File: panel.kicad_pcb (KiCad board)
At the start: 2 copper layers, 131.4 x 94 mm, 112 parts, among them J1 Conn_01x05, J2 Conn_01x05, J3 Screw_Terminal

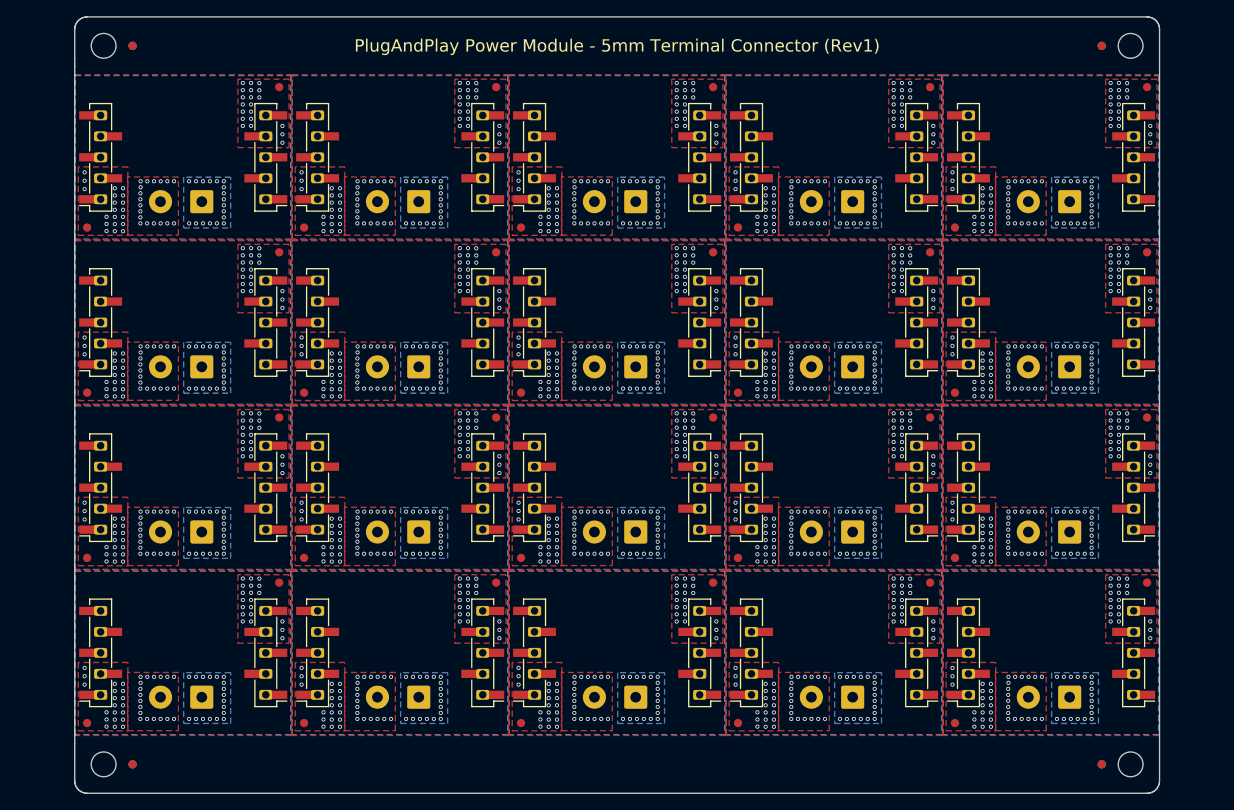
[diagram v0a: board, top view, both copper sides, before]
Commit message: Panel framing on all 4 sides
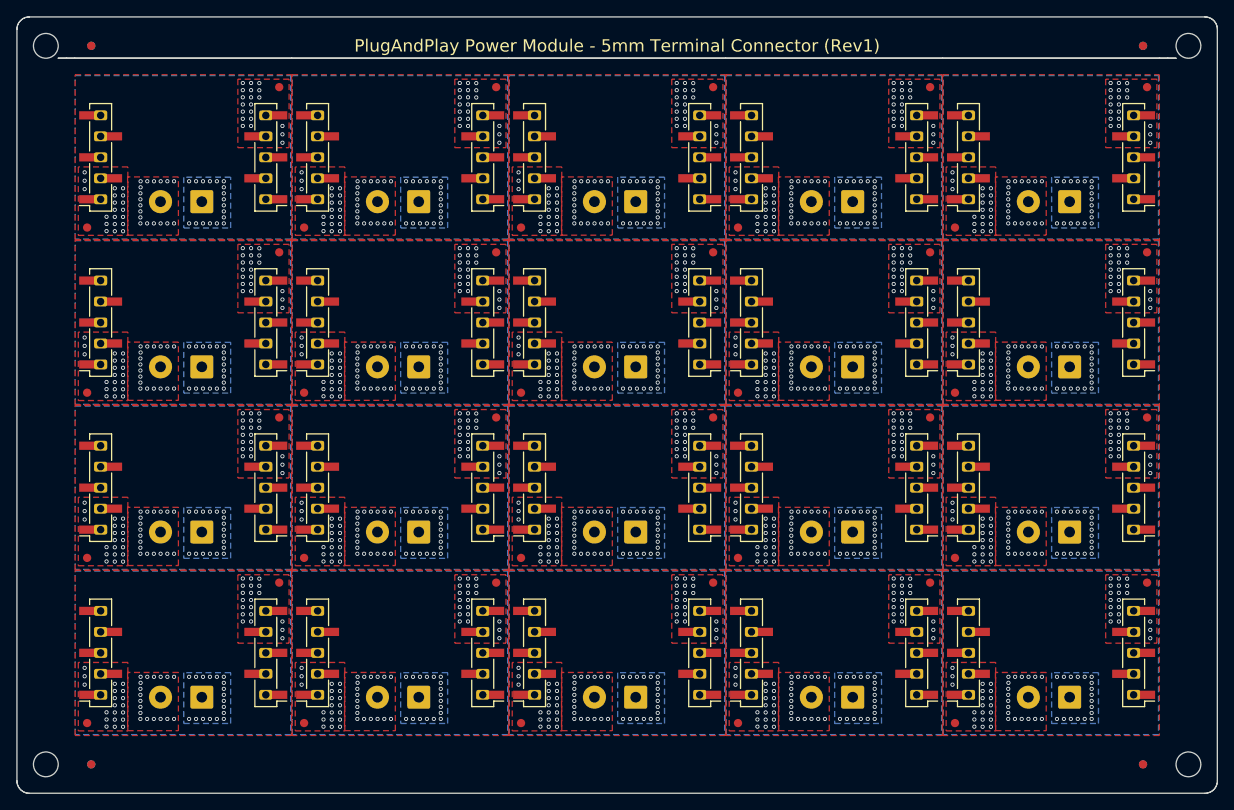
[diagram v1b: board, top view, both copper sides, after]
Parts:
- removed the J1 at (86.0, 57.0)
- removed the J1 at (164.8, 77.0)
- removed the J1 at (86.0, 37.0)
- removed the J1 at (164.8, 37.0)
- removed the J1 at (138.5, 37.0)
- removed the J1 at (112.2, 37.0)
- removed the J1 at (112.2, 57.0)
- removed the J1 at (86.0, 77.0)
- removed the J1 at (112.2, 97.0)
- removed the J1 at (191.0, 77.0)
- removed the J1 at (138.5, 77.0)
- removed the J1 at (138.5, 57.0)
- removed the J1 at (191.0, 37.0)
- removed the J1 at (112.2, 77.0)
- removed the J1 at (86.0, 97.0)
- removed the J1 at (164.8, 57.0)
- removed the J1 at (164.8, 97.0)
- removed the J1 at (191.0, 97.0)
- removed the J1 at (138.5, 97.0)
- removed the J1 at (191.0, 57.0)
- removed the J2 at (132.2, 37.0)
- removed the J2 at (106.0, 57.0)
- removed the J2 at (184.8, 97.0)
- removed the J2 at (158.5, 57.0)
- removed the J2 at (132.2, 77.0)
- removed the J2 at (211.0, 97.0)
- removed the J2 at (132.2, 97.0)
- removed the J2 at (184.8, 77.0)
- removed the J2 at (158.5, 97.0)
- removed the J2 at (132.2, 57.0)
- removed the J2 at (211.0, 57.0)
- removed the J2 at (184.8, 57.0)
- removed the J2 at (106.0, 97.0)
- removed the J2 at (106.0, 77.0)
- removed the J2 at (106.0, 37.0)
- removed the J2 at (184.8, 37.0)
- removed the J2 at (211.0, 37.0)
- removed the J2 at (158.5, 77.0)
- removed the J2 at (158.5, 37.0)
- removed the J2 at (211.0, 77.0)
- removed the J3 at (150.8, 42.4)
- removed the J3 at (124.5, 102.4)
- removed the J3 at (98.2, 82.4)
- removed the J3 at (124.5, 42.4)
- removed the J3 at (177.0, 42.4)
- removed the J3 at (203.3, 82.4)
- removed the J3 at (150.8, 62.4)
- removed the J3 at (124.5, 82.4)
- removed the J3 at (203.3, 102.4)
- removed the J3 at (177.0, 102.4)
- removed the J3 at (177.0, 82.4)
- removed the J3 at (150.8, 82.4)
- removed the J3 at (98.2, 62.4)
- removed the J3 at (98.2, 102.4)
- removed the J3 at (150.8, 102.4)
- removed the J3 at (124.5, 62.4)
- removed the J3 at (98.2, 42.4)
- removed the J3 at (203.3, 62.4)
- removed the J3 at (203.3, 42.4)
- removed the J3 at (177.0, 62.4)
- removed the REF** at (186.4, 68.5)
- removed the REF** at (160.1, 88.5)
- removed the REF** at (186.4, 48.5)
- removed the REF** at (163.1, 65.5)
- removed the REF** at (107.6, 68.5)
- removed the REF** at (212.7, 88.5)
- removed the REF** at (110.6, 65.5)
- removed the REF** at (189.4, 105.5)
- removed the REF** at (84.3, 85.5)
- removed the REF** at (133.9, 88.5)
- removed the REF** at (107.6, 48.5)
- removed the REF** at (84.3, 45.5)
- removed the REF** at (136.9, 85.5)
- removed the REF** at (160.1, 28.5)
- removed the REF** at (163.1, 105.5)
- removed the REF** at (212.7, 68.5)
- removed the REF** at (189.4, 65.5)
- removed the REF** at (110.6, 85.5)
- removed the REF** at (84.3, 105.5)
- removed the REF** at (133.9, 28.5)
- removed the REF** at (212.7, 48.5)
- removed the REF** at (163.1, 45.5)
- removed the REF** at (133.9, 68.5)
- removed the REF** at (110.6, 45.5)
- removed the REF** at (107.6, 88.5)
- removed the REF** at (212.7, 28.5)
- removed the REF** at (136.9, 45.5)
- removed the REF** at (189.4, 45.5)
- removed the REF** at (133.9, 48.5)
- removed the REF** at (160.1, 48.5)
- removed the REF** at (186.4, 88.5)
- removed the REF** at (136.9, 65.5)
- removed the REF** at (136.9, 105.5)
- removed the REF** at (163.1, 85.5)
- removed the REF** at (84.3, 65.5)
- removed the REF** at (160.1, 68.5)
- removed the REF** at (186.4, 28.5)
- removed the REF** at (107.6, 28.5)
- removed the REF** at (110.6, 105.5)
- removed the REF** at (189.4, 85.5)
- added J1: Conn_01x05, Library:PinSocket_1x05_P2.54mm_Vertical_SMD_Pin1Right, F.Cu at (164.8, 37.0)
- added J1: Conn_01x05, Library:PinSocket_1x05_P2.54mm_Vertical_SMD_Pin1Right, F.Cu at (86.0, 57.0)
- added J1: Conn_01x05, Library:PinSocket_1x05_P2.54mm_Vertical_SMD_Pin1Right, F.Cu at (191.0, 37.0)
- added J1: Conn_01x05, Library:PinSocket_1x05_P2.54mm_Vertical_SMD_Pin1Right, F.Cu at (86.0, 97.0)
- added J1: Conn_01x05, Library:PinSocket_1x05_P2.54mm_Vertical_SMD_Pin1Right, F.Cu at (138.5, 77.0)
- added J1: Conn_01x05, Library:PinSocket_1x05_P2.54mm_Vertical_SMD_Pin1Right, F.Cu at (164.8, 57.0)
- added J1: Conn_01x05, Library:PinSocket_1x05_P2.54mm_Vertical_SMD_Pin1Right, F.Cu at (112.2, 97.0)
- added J1: Conn_01x05, Library:PinSocket_1x05_P2.54mm_Vertical_SMD_Pin1Right, F.Cu at (86.0, 77.0)
- added J1: Conn_01x05, Library:PinSocket_1x05_P2.54mm_Vertical_SMD_Pin1Right, F.Cu at (138.5, 97.0)
- added J1: Conn_01x05, Library:PinSocket_1x05_P2.54mm_Vertical_SMD_Pin1Right, F.Cu at (164.8, 77.0)
- added J1: Conn_01x05, Library:PinSocket_1x05_P2.54mm_Vertical_SMD_Pin1Right, F.Cu at (138.5, 57.0)
- added J1: Conn_01x05, Library:PinSocket_1x05_P2.54mm_Vertical_SMD_Pin1Right, F.Cu at (191.0, 77.0)
- added J1: Conn_01x05, Library:PinSocket_1x05_P2.54mm_Vertical_SMD_Pin1Right, F.Cu at (112.2, 77.0)
- added J1: Conn_01x05, Library:PinSocket_1x05_P2.54mm_Vertical_SMD_Pin1Right, F.Cu at (112.2, 57.0)
- added J1: Conn_01x05, Library:PinSocket_1x05_P2.54mm_Vertical_SMD_Pin1Right, F.Cu at (191.0, 57.0)
- added J1: Conn_01x05, Library:PinSocket_1x05_P2.54mm_Vertical_SMD_Pin1Right, F.Cu at (86.0, 37.0)
- added J1: Conn_01x05, Library:PinSocket_1x05_P2.54mm_Vertical_SMD_Pin1Right, F.Cu at (138.5, 37.0)
- added J1: Conn_01x05, Library:PinSocket_1x05_P2.54mm_Vertical_SMD_Pin1Right, F.Cu at (164.8, 97.0)
- added J1: Conn_01x05, Library:PinSocket_1x05_P2.54mm_Vertical_SMD_Pin1Right, F.Cu at (191.0, 97.0)
- added J1: Conn_01x05, Library:PinSocket_1x05_P2.54mm_Vertical_SMD_Pin1Right, F.Cu at (112.2, 37.0)
- added J2: Conn_01x05, Library:PinSocket_1x05_P2.54mm_Vertical_SMD_Pin1Left, F.Cu at (211.0, 77.0)
- added J2: Conn_01x05, Library:PinSocket_1x05_P2.54mm_Vertical_SMD_Pin1Left, F.Cu at (132.2, 97.0)
- added J2: Conn_01x05, Library:PinSocket_1x05_P2.54mm_Vertical_SMD_Pin1Left, F.Cu at (184.8, 97.0)
- added J2: Conn_01x05, Library:PinSocket_1x05_P2.54mm_Vertical_SMD_Pin1Left, F.Cu at (158.5, 37.0)
- added J2: Conn_01x05, Library:PinSocket_1x05_P2.54mm_Vertical_SMD_Pin1Left, F.Cu at (132.2, 37.0)
- added J2: Conn_01x05, Library:PinSocket_1x05_P2.54mm_Vertical_SMD_Pin1Left, F.Cu at (158.5, 77.0)
- added J2: Conn_01x05, Library:PinSocket_1x05_P2.54mm_Vertical_SMD_Pin1Left, F.Cu at (184.8, 57.0)
- added J2: Conn_01x05, Library:PinSocket_1x05_P2.54mm_Vertical_SMD_Pin1Left, F.Cu at (211.0, 37.0)
- added J2: Conn_01x05, Library:PinSocket_1x05_P2.54mm_Vertical_SMD_Pin1Left, F.Cu at (211.0, 57.0)
- added J2: Conn_01x05, Library:PinSocket_1x05_P2.54mm_Vertical_SMD_Pin1Left, F.Cu at (106.0, 97.0)
- added J2: Conn_01x05, Library:PinSocket_1x05_P2.54mm_Vertical_SMD_Pin1Left, F.Cu at (132.2, 77.0)
- added J2: Conn_01x05, Library:PinSocket_1x05_P2.54mm_Vertical_SMD_Pin1Left, F.Cu at (106.0, 37.0)
- added J2: Conn_01x05, Library:PinSocket_1x05_P2.54mm_Vertical_SMD_Pin1Left, F.Cu at (106.0, 77.0)
- added J2: Conn_01x05, Library:PinSocket_1x05_P2.54mm_Vertical_SMD_Pin1Left, F.Cu at (106.0, 57.0)
- added J2: Conn_01x05, Library:PinSocket_1x05_P2.54mm_Vertical_SMD_Pin1Left, F.Cu at (184.8, 77.0)
- added J2: Conn_01x05, Library:PinSocket_1x05_P2.54mm_Vertical_SMD_Pin1Left, F.Cu at (158.5, 97.0)
- added J2: Conn_01x05, Library:PinSocket_1x05_P2.54mm_Vertical_SMD_Pin1Left, F.Cu at (184.8, 37.0)
- added J2: Conn_01x05, Library:PinSocket_1x05_P2.54mm_Vertical_SMD_Pin1Left, F.Cu at (158.5, 57.0)
- added J2: Conn_01x05, Library:PinSocket_1x05_P2.54mm_Vertical_SMD_Pin1Left, F.Cu at (132.2, 57.0)
- added J2: Conn_01x05, Library:PinSocket_1x05_P2.54mm_Vertical_SMD_Pin1Left, F.Cu at (211.0, 97.0)
- added J3: Screw_Terminal, TerminalBlock:TerminalBlock_MaiXu_MX126-5.0-02P_1x02_P5.00mm, B.Cu at (124.5, 102.4)
- added J3: Screw_Terminal, TerminalBlock:TerminalBlock_MaiXu_MX126-5.0-02P_1x02_P5.00mm, B.Cu at (177.0, 102.4)
- added J3: Screw_Terminal, TerminalBlock:TerminalBlock_MaiXu_MX126-5.0-02P_1x02_P5.00mm, B.Cu at (150.8, 62.4)
- added J3: Screw_Terminal, TerminalBlock:TerminalBlock_MaiXu_MX126-5.0-02P_1x02_P5.00mm, B.Cu at (177.0, 62.4)
- added J3: Screw_Terminal, TerminalBlock:TerminalBlock_MaiXu_MX126-5.0-02P_1x02_P5.00mm, B.Cu at (203.3, 42.4)
- added J3: Screw_Terminal, TerminalBlock:TerminalBlock_MaiXu_MX126-5.0-02P_1x02_P5.00mm, B.Cu at (203.3, 62.4)
- added J3: Screw_Terminal, TerminalBlock:TerminalBlock_MaiXu_MX126-5.0-02P_1x02_P5.00mm, B.Cu at (98.2, 102.4)
- added J3: Screw_Terminal, TerminalBlock:TerminalBlock_MaiXu_MX126-5.0-02P_1x02_P5.00mm, B.Cu at (177.0, 82.4)
- added J3: Screw_Terminal, TerminalBlock:TerminalBlock_MaiXu_MX126-5.0-02P_1x02_P5.00mm, B.Cu at (150.8, 82.4)
- added J3: Screw_Terminal, TerminalBlock:TerminalBlock_MaiXu_MX126-5.0-02P_1x02_P5.00mm, B.Cu at (177.0, 42.4)
- added J3: Screw_Terminal, TerminalBlock:TerminalBlock_MaiXu_MX126-5.0-02P_1x02_P5.00mm, B.Cu at (150.8, 102.4)
- added J3: Screw_Terminal, TerminalBlock:TerminalBlock_MaiXu_MX126-5.0-02P_1x02_P5.00mm, B.Cu at (150.8, 42.4)
- added J3: Screw_Terminal, TerminalBlock:TerminalBlock_MaiXu_MX126-5.0-02P_1x02_P5.00mm, B.Cu at (124.5, 42.4)
- added J3: Screw_Terminal, TerminalBlock:TerminalBlock_MaiXu_MX126-5.0-02P_1x02_P5.00mm, B.Cu at (203.3, 82.4)
- added J3: Screw_Terminal, TerminalBlock:TerminalBlock_MaiXu_MX126-5.0-02P_1x02_P5.00mm, B.Cu at (124.5, 62.4)
- added J3: Screw_Terminal, TerminalBlock:TerminalBlock_MaiXu_MX126-5.0-02P_1x02_P5.00mm, B.Cu at (98.2, 62.4)
- added J3: Screw_Terminal, TerminalBlock:TerminalBlock_MaiXu_MX126-5.0-02P_1x02_P5.00mm, B.Cu at (203.3, 102.4)
- added J3: Screw_Terminal, TerminalBlock:TerminalBlock_MaiXu_MX126-5.0-02P_1x02_P5.00mm, B.Cu at (98.2, 82.4)
- added J3: Screw_Terminal, TerminalBlock:TerminalBlock_MaiXu_MX126-5.0-02P_1x02_P5.00mm, B.Cu at (98.2, 42.4)
- added J3: Screw_Terminal, TerminalBlock:TerminalBlock_MaiXu_MX126-5.0-02P_1x02_P5.00mm, B.Cu at (124.5, 82.4)
- added REF**: Fiducial_1mm_Mask2mm, Fiducial:Fiducial_1mm_Mask2mm, F.Cu at (133.9, 88.5)
- added REF**: Fiducial_1mm_Mask2mm, Fiducial:Fiducial_1mm_Mask2mm, F.Cu at (212.7, 68.5)
- added REF**: Fiducial_1mm_Mask2mm, Fiducial:Fiducial_1mm_Mask2mm, F.Cu at (110.6, 105.5)
- added REF**: Fiducial_1mm_Mask2mm, Fiducial:Fiducial_1mm_Mask2mm, F.Cu at (110.6, 65.5)
- added REF**: Fiducial_1mm_Mask2mm, Fiducial:Fiducial_1mm_Mask2mm, F.Cu at (186.4, 68.5)
- added REF**: Fiducial_1mm_Mask2mm, Fiducial:Fiducial_1mm_Mask2mm, F.Cu at (136.9, 45.5)
- added REF**: Fiducial_1mm_Mask2mm, Fiducial:Fiducial_1mm_Mask2mm, F.Cu at (136.9, 65.5)
- added REF**: Fiducial_1mm_Mask2mm, Fiducial:Fiducial_1mm_Mask2mm, F.Cu at (133.9, 48.5)
- added REF**: Fiducial_1mm_Mask2mm, Fiducial:Fiducial_1mm_Mask2mm, F.Cu at (212.7, 28.5)
- added REF**: Fiducial_1mm_Mask2mm, Fiducial:Fiducial_1mm_Mask2mm, F.Cu at (163.1, 85.5)
- added REF**: Fiducial_1mm_Mask2mm, Fiducial:Fiducial_1mm_Mask2mm, F.Cu at (107.6, 48.5)
- added REF**: Fiducial_1mm_Mask2mm, Fiducial:Fiducial_1mm_Mask2mm, F.Cu at (160.1, 68.5)
- added REF**: Fiducial_1mm_Mask2mm, Fiducial:Fiducial_1mm_Mask2mm, F.Cu at (212.7, 48.5)
- added REF**: Fiducial_1mm_Mask2mm, Fiducial:Fiducial_1mm_Mask2mm, F.Cu at (186.4, 28.5)
- added REF**: Fiducial_1mm_Mask2mm, Fiducial:Fiducial_1mm_Mask2mm, F.Cu at (84.3, 85.5)
- added REF**: Fiducial_1mm_Mask2mm, Fiducial:Fiducial_1mm_Mask2mm, F.Cu at (163.1, 65.5)
- added REF**: Fiducial_1mm_Mask2mm, Fiducial:Fiducial_1mm_Mask2mm, F.Cu at (189.4, 65.5)
- added REF**: Fiducial_1mm_Mask2mm, Fiducial:Fiducial_1mm_Mask2mm, F.Cu at (160.1, 88.5)
- added REF**: Fiducial_1mm_Mask2mm, Fiducial:Fiducial_1mm_Mask2mm, F.Cu at (160.1, 28.5)
- added REF**: Fiducial_1mm_Mask2mm, Fiducial:Fiducial_1mm_Mask2mm, F.Cu at (107.6, 68.5)
- added REF**: Fiducial_1mm_Mask2mm, Fiducial:Fiducial_1mm_Mask2mm, F.Cu at (163.1, 45.5)
- added REF**: Fiducial_1mm_Mask2mm, Fiducial:Fiducial_1mm_Mask2mm, F.Cu at (110.6, 85.5)
- added REF**: Fiducial_1mm_Mask2mm, Fiducial:Fiducial_1mm_Mask2mm, F.Cu at (212.7, 88.5)
- added REF**: Fiducial_1mm_Mask2mm, Fiducial:Fiducial_1mm_Mask2mm, F.Cu at (136.9, 105.5)
- added REF**: Fiducial_1mm_Mask2mm, Fiducial:Fiducial_1mm_Mask2mm, F.Cu at (186.4, 88.5)
- added REF**: Fiducial_1mm_Mask2mm, Fiducial:Fiducial_1mm_Mask2mm, F.Cu at (84.3, 65.5)
- added REF**: Fiducial_1mm_Mask2mm, Fiducial:Fiducial_1mm_Mask2mm, F.Cu at (163.1, 105.5)
- added REF**: Fiducial_1mm_Mask2mm, Fiducial:Fiducial_1mm_Mask2mm, F.Cu at (107.6, 28.5)
- added REF**: Fiducial_1mm_Mask2mm, Fiducial:Fiducial_1mm_Mask2mm, F.Cu at (189.4, 45.5)
- added REF**: Fiducial_1mm_Mask2mm, Fiducial:Fiducial_1mm_Mask2mm, F.Cu at (84.3, 45.5)
- added REF**: Fiducial_1mm_Mask2mm, Fiducial:Fiducial_1mm_Mask2mm, F.Cu at (136.9, 85.5)
- added REF**: Fiducial_1mm_Mask2mm, Fiducial:Fiducial_1mm_Mask2mm, F.Cu at (133.9, 68.5)
- added REF**: Fiducial_1mm_Mask2mm, Fiducial:Fiducial_1mm_Mask2mm, F.Cu at (189.4, 85.5)
- added REF**: Fiducial_1mm_Mask2mm, Fiducial:Fiducial_1mm_Mask2mm, F.Cu at (186.4, 48.5)
- added REF**: Fiducial_1mm_Mask2mm, Fiducial:Fiducial_1mm_Mask2mm, F.Cu at (160.1, 48.5)
- added REF**: Fiducial_1mm_Mask2mm, Fiducial:Fiducial_1mm_Mask2mm, F.Cu at (107.6, 88.5)
- added REF**: Fiducial_1mm_Mask2mm, Fiducial:Fiducial_1mm_Mask2mm, F.Cu at (133.9, 28.5)
- added REF**: Fiducial_1mm_Mask2mm, Fiducial:Fiducial_1mm_Mask2mm, F.Cu at (189.4, 105.5)
- added REF**: Fiducial_1mm_Mask2mm, Fiducial:Fiducial_1mm_Mask2mm, F.Cu at (84.3, 105.5)
- added REF**: Fiducial_1mm_Mask2mm, Fiducial:Fiducial_1mm_Mask2mm, F.Cu at (110.6, 45.5)
- moved KiKit_TO_3 7.00 mm to (79.3, 110.5)
- moved KiKit_TO_4 7.00 mm to (217.7, 110.5)
- moved KiKit_TO_1 7.00 mm to (79.3, 23.5)
- moved KiKit_TO_2 7.00 mm to (217.7, 23.5)
- moved KiKit_FID_B_3 5.00 mm to (84.8, 110.5)
- moved KiKit_FID_B_4 5.00 mm to (212.2, 110.5)
- moved KiKit_FID_T_3 5.00 mm to (84.8, 110.5)
- moved KiKit_FID_T_4 5.00 mm to (212.2, 110.5)
- moved KiKit_FID_B_1 5.00 mm to (84.8, 23.5)
- moved KiKit_FID_B_2 5.00 mm to (212.2, 23.5)
- moved KiKit_FID_T_1 5.00 mm to (84.8, 23.5)
- moved KiKit_FID_T_2 5.00 mm to (212.2, 23.5)
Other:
- board size 131.4 x 94 mm -> 145.4 x 94 mm

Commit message: Increase header connectors paste openning by 5%. Decrease screw terminal holes from 2.3mm to 2.2mm.
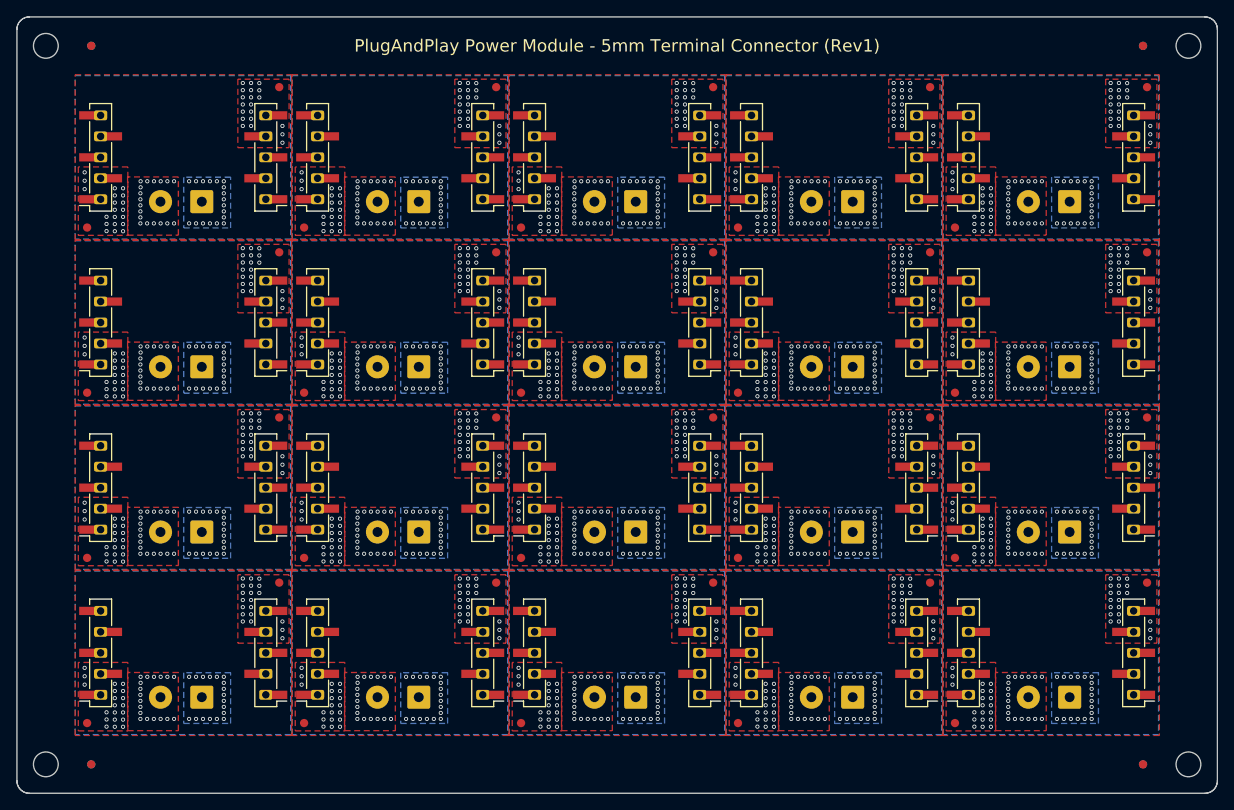
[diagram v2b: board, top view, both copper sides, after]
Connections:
- net Board_0-unconnected-(J1-Pin_3-Pad3)_1 renamed Board_0-unconnected-(J1-Pin_3-Pad3)
- net Board_0-unconnected-(J2-Pin_3-Pad3)_1 renamed Board_0-unconnected-(J2-Pin_3-Pad3)
- net Board_1-unconnected-(J1-Pin_3-Pad3)_1 renamed Board_1-unconnected-(J1-Pin_3-Pad3)
- net Board_1-unconnected-(J2-Pin_3-Pad3)_1 renamed Board_1-unconnected-(J2-Pin_3-Pad3)
- net Board_10-unconnected-(J1-Pin_3-Pad3)_1 renamed Board_10-unconnected-(J1-Pin_3-Pad3)
- net Board_10-unconnected-(J2-Pin_3-Pad3)_1 renamed Board_10-unconnected-(J2-Pin_3-Pad3)
- net Board_11-unconnected-(J1-Pin_3-Pad3)_1 renamed Board_11-unconnected-(J1-Pin_3-Pad3)
- net Board_11-unconnected-(J2-Pin_3-Pad3)_1 renamed Board_11-unconnected-(J2-Pin_3-Pad3)
- net Board_12-unconnected-(J1-Pin_3-Pad3)_1 renamed Board_12-unconnected-(J1-Pin_3-Pad3)
- net Board_12-unconnected-(J2-Pin_3-Pad3)_1 renamed Board_12-unconnected-(J2-Pin_3-Pad3)
- net Board_13-unconnected-(J1-Pin_3-Pad3)_1 renamed Board_13-unconnected-(J1-Pin_3-Pad3)
- net Board_13-unconnected-(J2-Pin_3-Pad3)_1 renamed Board_13-unconnected-(J2-Pin_3-Pad3)
- net Board_14-unconnected-(J1-Pin_3-Pad3)_1 renamed Board_14-unconnected-(J1-Pin_3-Pad3)
- net Board_14-unconnected-(J2-Pin_3-Pad3)_1 renamed Board_14-unconnected-(J2-Pin_3-Pad3)
- net Board_15-unconnected-(J1-Pin_3-Pad3)_1 renamed Board_15-unconnected-(J1-Pin_3-Pad3)
- net Board_15-unconnected-(J2-Pin_3-Pad3)_1 renamed Board_15-unconnected-(J2-Pin_3-Pad3)
- net Board_16-unconnected-(J1-Pin_3-Pad3)_1 renamed Board_16-unconnected-(J1-Pin_3-Pad3)
- net Board_16-unconnected-(J2-Pin_3-Pad3)_1 renamed Board_16-unconnected-(J2-Pin_3-Pad3)
- net Board_17-unconnected-(J1-Pin_3-Pad3)_1 renamed Board_17-unconnected-(J1-Pin_3-Pad3)
- net Board_17-unconnected-(J2-Pin_3-Pad3)_1 renamed Board_17-unconnected-(J2-Pin_3-Pad3)
- net Board_18-unconnected-(J1-Pin_3-Pad3)_1 renamed Board_18-unconnected-(J1-Pin_3-Pad3)
- net Board_18-unconnected-(J2-Pin_3-Pad3)_1 renamed Board_18-unconnected-(J2-Pin_3-Pad3)
- net Board_19-unconnected-(J1-Pin_3-Pad3)_1 renamed Board_19-unconnected-(J1-Pin_3-Pad3)
- net Board_19-unconnected-(J2-Pin_3-Pad3)_1 renamed Board_19-unconnected-(J2-Pin_3-Pad3)
- net Board_2-unconnected-(J1-Pin_3-Pad3)_1 renamed Board_2-unconnected-(J1-Pin_3-Pad3)
- net Board_2-unconnected-(J2-Pin_3-Pad3)_1 renamed Board_2-unconnected-(J2-Pin_3-Pad3)
- net Board_3-unconnected-(J1-Pin_3-Pad3)_1 renamed Board_3-unconnected-(J1-Pin_3-Pad3)
- net Board_3-unconnected-(J2-Pin_3-Pad3)_1 renamed Board_3-unconnected-(J2-Pin_3-Pad3)
- net Board_4-unconnected-(J1-Pin_3-Pad3)_1 renamed Board_4-unconnected-(J1-Pin_3-Pad3)
- net Board_4-unconnected-(J2-Pin_3-Pad3)_1 renamed Board_4-unconnected-(J2-Pin_3-Pad3)
- net Board_5-unconnected-(J1-Pin_3-Pad3)_1 renamed Board_5-unconnected-(J1-Pin_3-Pad3)
- net Board_5-unconnected-(J2-Pin_3-Pad3)_1 renamed Board_5-unconnected-(J2-Pin_3-Pad3)
- net Board_6-unconnected-(J1-Pin_3-Pad3)_1 renamed Board_6-unconnected-(J1-Pin_3-Pad3)
- net Board_6-unconnected-(J2-Pin_3-Pad3)_1 renamed Board_6-unconnected-(J2-Pin_3-Pad3)
- net Board_7-unconnected-(J1-Pin_3-Pad3)_1 renamed Board_7-unconnected-(J1-Pin_3-Pad3)
- net Board_7-unconnected-(J2-Pin_3-Pad3)_1 renamed Board_7-unconnected-(J2-Pin_3-Pad3)
- net Board_8-unconnected-(J1-Pin_3-Pad3)_1 renamed Board_8-unconnected-(J1-Pin_3-Pad3)
- net Board_8-unconnected-(J2-Pin_3-Pad3)_1 renamed Board_8-unconnected-(J2-Pin_3-Pad3)
- net Board_9-unconnected-(J1-Pin_3-Pad3)_1 renamed Board_9-unconnected-(J1-Pin_3-Pad3)
- net Board_9-unconnected-(J2-Pin_3-Pad3)_1 renamed Board_9-unconnected-(J2-Pin_3-Pad3)
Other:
- outline, holes or cut-outs redrawn
